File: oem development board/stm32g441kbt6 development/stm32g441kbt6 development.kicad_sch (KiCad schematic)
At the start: 22 parts, among them J1 CONN_pcie_x1, J2 Programming_Pin_Header, SW1 INTERRUPT TEST SWITCH, U1 STM32G441KBT6, U2 MCP2561-E_SN, U3 SPX3819M5-L-3-3_TR, Y1 X_Crystal_16MHz_18pF

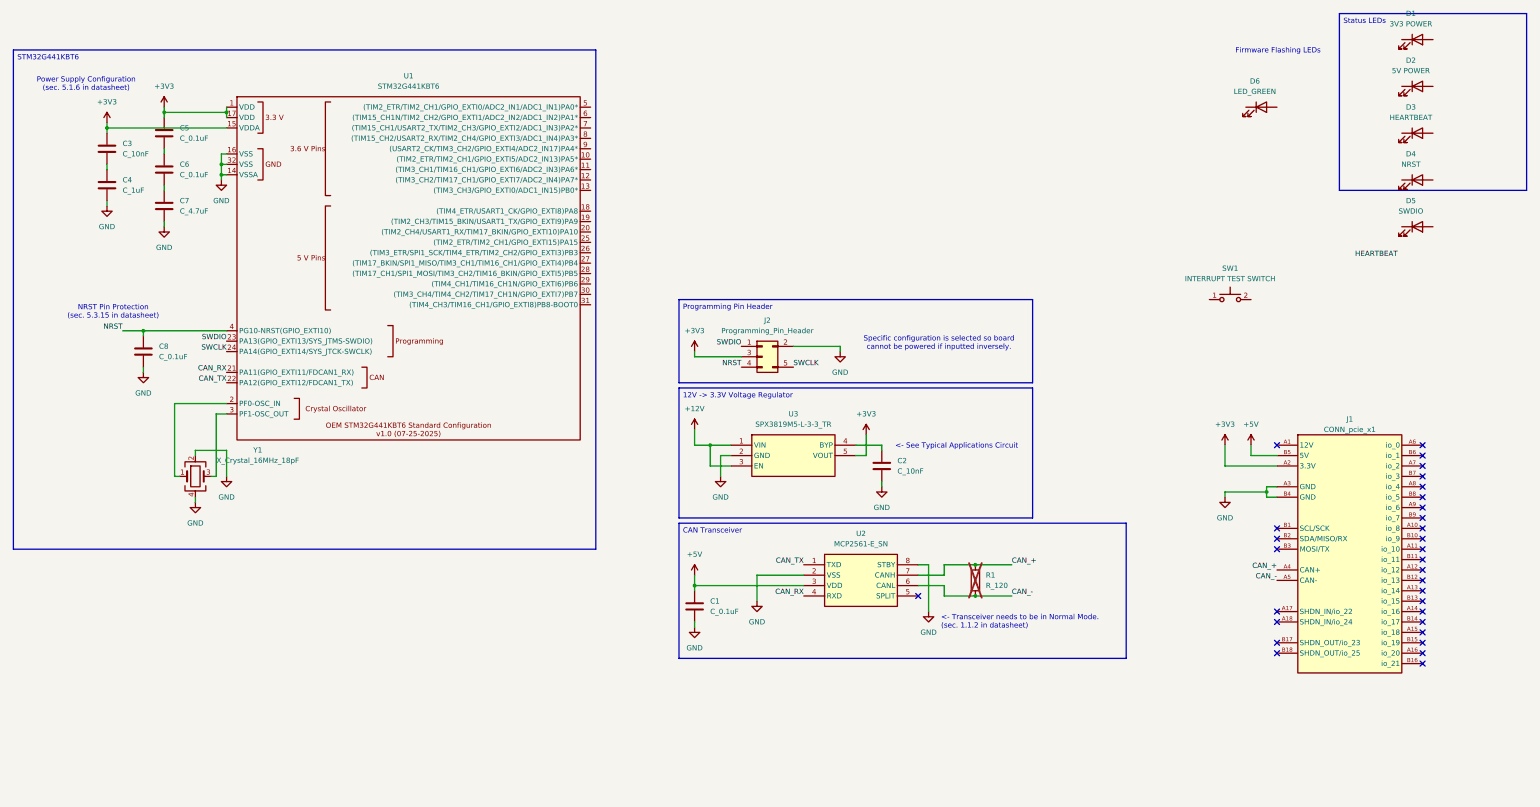
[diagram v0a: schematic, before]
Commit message: Added Debug LEDs, Some Test Points, Minor changes to STM32G441KBT6 symbol
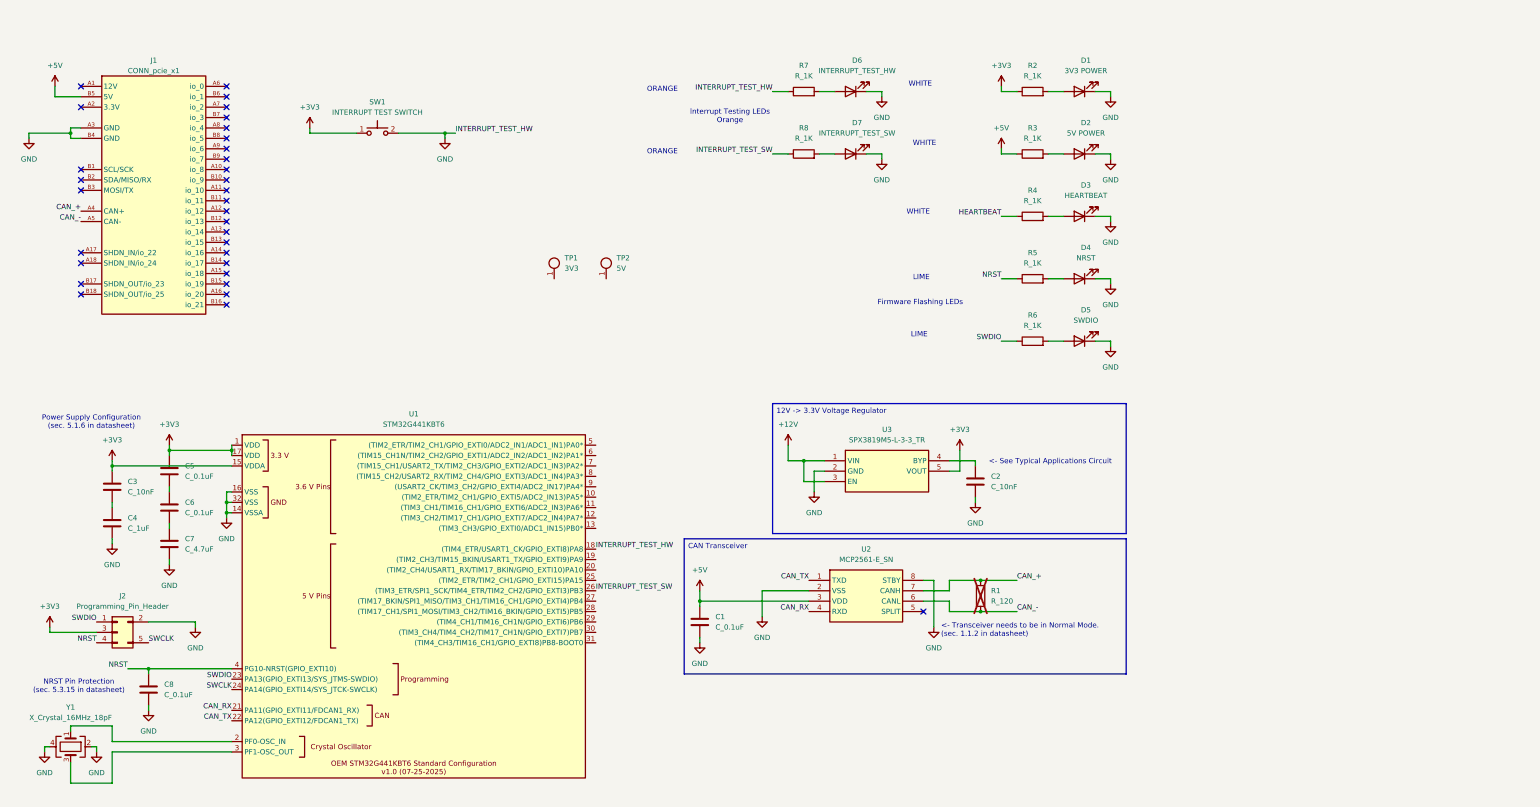
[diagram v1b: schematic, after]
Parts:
- removed D6: LED_GREEN, OEM:CHIPLED_0805, symbol OEM:LED_GREEN
- added D6: INTERRUPT_TEST_HW, OEM:CHIPLED_0805, symbol OEM:LED_AMBER
- added D7: INTERRUPT_TEST_SW, OEM:CHIPLED_0805, symbol OEM:LED_AMBER
- added R2, R3, R4, R5, R6, R7, R8: R_1K, OEM:R_0603, symbol OEM:R_1K
- added TP1: 3V3, OEM:Test_Point_SMD, symbol OEM:TP_SMD
- added TP2: 5V, OEM:Test_Point_SMD, symbol OEM:TP_SMD
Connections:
- net +3V3: now also SW1.1, R2.1; no longer J1.A2 (3.3V)
- net +5V: now also R3.1
- net GND: now also D1.1 (K), D2.1 (K), D3.1 (K), D4.1 (K), D5.1 (K), SW1.2, U1.18 ((TIM4_ETR/USART1_CK/GPIO_EXTI8)PA8), D6.1 (K), D7.1 (K), R7.1
- net HEARTBEAT: now also R4.1
- net NRST: now also R5.1
- net SWDIO: now also R6.1
- net at D2.2 (A): now also R3.2
- net at D3.2 (A): now also R4.2
- net at D4.2 (A): now also R5.2
- net at D1.2 (A): now also R2.2
- net INTERRUPT_TEST_SW: now reaches U1.26 ((TIM3_ETR/SPI1_SCK/TIM4_ETR/TIM2_CH2/GPIO_EXTI3)PB3)
- net INTERRUPT_TEST_SW: now also R8.1
- net at D5.2 (A): now also R6.2
- new net: D6.2 (A), R7.2
- new net: D7.2 (A), R8.2
- no-connect marks 31 -> 32
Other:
- note added: "Interrupt Testing LEDs Orange"
- note added: "LIME"
- note added: "ORANGE"
- note added: "WHITE"
- note removed: "Specific configuration is selected so board cannot be powered if inputted inversely."
- moved on the sheet: C1, C2, C3, C4, C5, C6, C7, C8, D1, D2, D3, D4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

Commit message: Condensed Symbol Design; Slight changes to development board
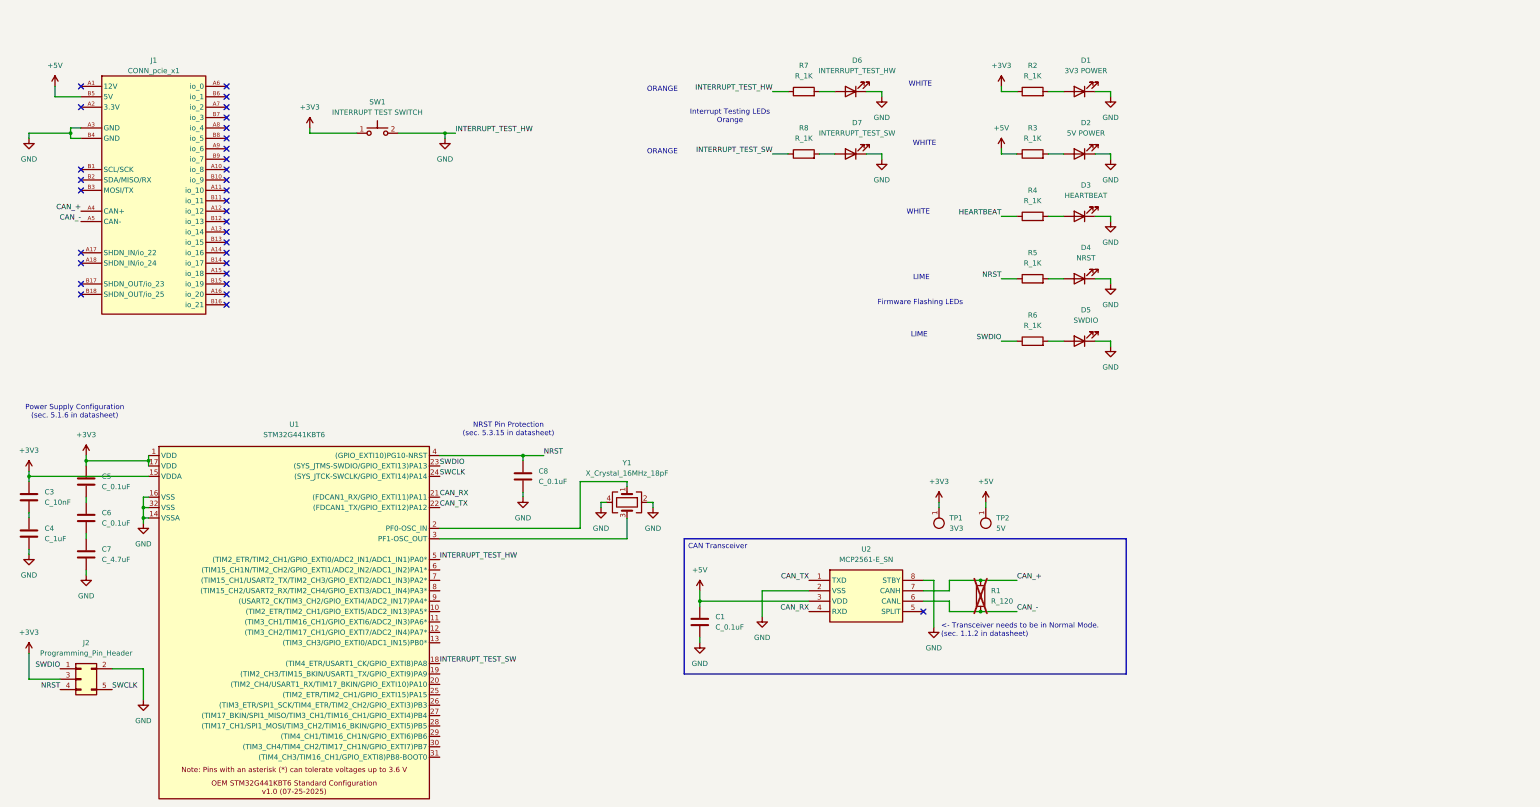
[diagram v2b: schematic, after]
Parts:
- removed C2: C_10nF, OEM:C_0603, symbol OEM:C_10nF
- removed U3: SPX3819M5-L-3-3_TR, stm32g441kbt6:SOIC127P600X175-8N, symbol stm32g441kb:SPX3819M5-L-3-3_TR
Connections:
- net +3V3: now also TP1.1
- net +5V: now also TP2.1
- net GND: now also U1.5 ((TIM2_ETR/TIM2_CH1/GPIO_EXTI0/ADC2_IN1/ADC1_IN1)PA0*); no longer U1.18 ((TIM4_ETR/USART1_CK/GPIO_EXTI8)PA8)
- net INTERRUPT_TEST_SW: now also U1.18 ((TIM4_ETR/USART1_CK/GPIO_EXTI8)PA8); no longer U1.26 ((TIM3_ETR/SPI1_SCK/TIM4_ETR/TIM2_CH2/GPIO_EXTI3)PB3)
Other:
- note removed: "<- See Typical Applications Circuit"
- moved on the sheet: C3, C4, C5, C6, C7, C8, J2, TP1, TP2, Y1

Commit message: Added footprints for new voltage regulator components, added test points and other things
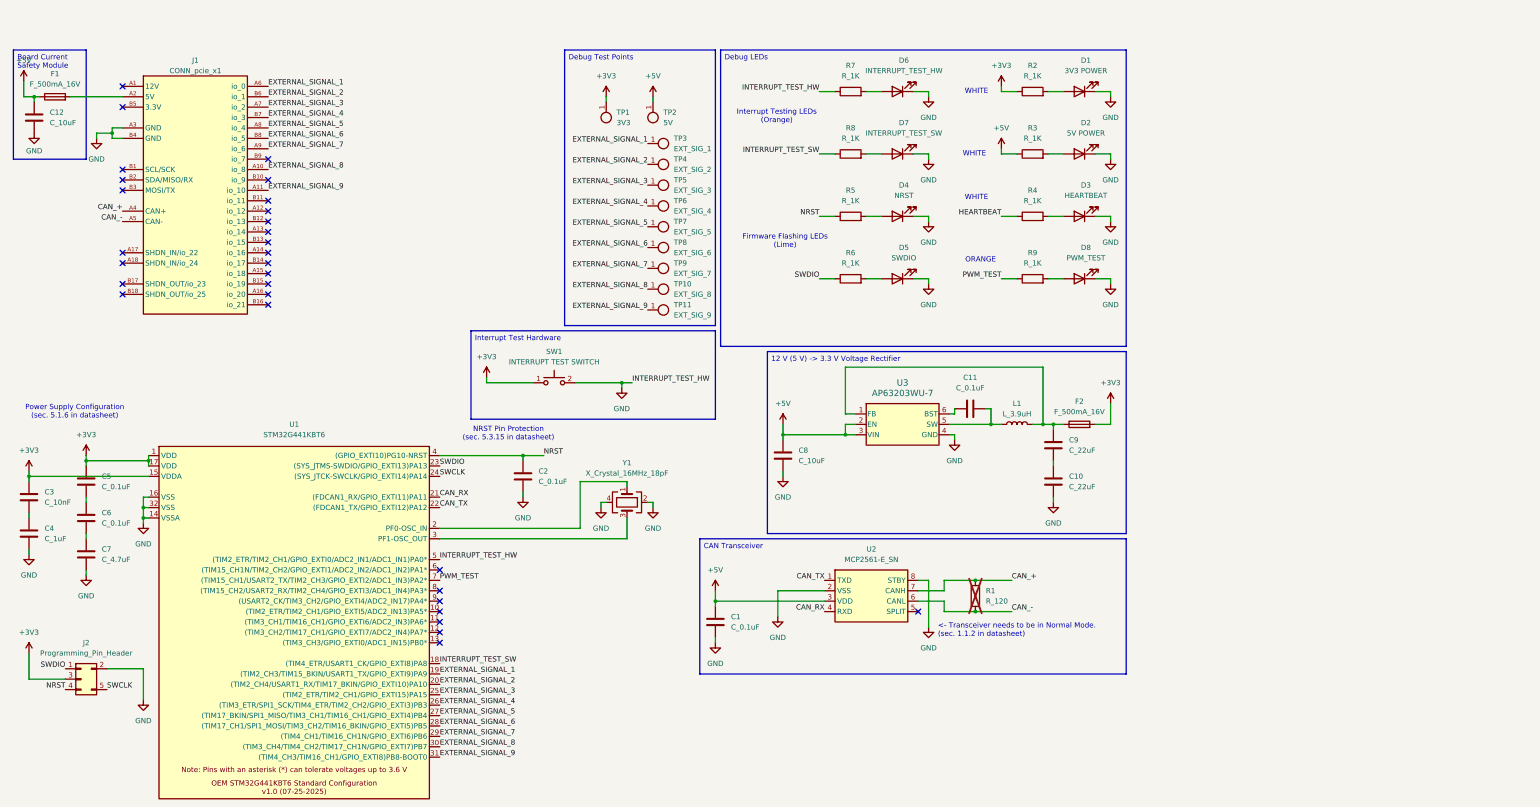
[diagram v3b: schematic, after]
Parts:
- added C10, C9: C_22uF, Capacitor_SMD:C_1206_3216Metric, symbol OEM:C_22uF
- added C11: C_0.1uF, OEM:C_0603, symbol OEM:C_0.1uF
- added C12, C8: C_10uF, OEM:C_0603, symbol OEM:C_10uF
- added D8: PWM_TEST, OEM:CHIPLED_0805, symbol OEM:LED_AMBER
- added F1, F2: F_500mA_16V, OEM:Fuse_1210, symbol OEM:F_500mA_16V
- added L1: L_3.9uH, stm32g441kbt6:IND_BOURNS_SRR5018, symbol stm32g441kb:L_3.9uH
- added R9: R_1K, OEM:R_0603, symbol OEM:R_1K
- added TP10: EXT_SIG_8, OEM:Test_Point_SMD, symbol OEM:TP_SMD
- added TP11: EXT_SIG_9, OEM:Test_Point_SMD, symbol OEM:TP_SMD
- added TP3: EXT_SIG_1, OEM:Test_Point_SMD, symbol OEM:TP_SMD
- added TP4: EXT_SIG_2, OEM:Test_Point_SMD, symbol OEM:TP_SMD
- added TP5: EXT_SIG_3, OEM:Test_Point_SMD, symbol OEM:TP_SMD
- added TP6: EXT_SIG_4, OEM:Test_Point_SMD, symbol OEM:TP_SMD
- added TP7: EXT_SIG_5, OEM:Test_Point_SMD, symbol OEM:TP_SMD
- added TP8: EXT_SIG_6, OEM:Test_Point_SMD, symbol OEM:TP_SMD
- added TP9: EXT_SIG_7, OEM:Test_Point_SMD, symbol OEM:TP_SMD
- added U3: AP63203WU-7, stm32g441kbt6:AP63203WU-7_DIO, symbol stm32g441kb:AP63203WU-7
- J1: footprint OEM:te_pcie_x1_connector -> OEM:pcie_x1
- renumbered C8 to C2
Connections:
- net +3V3: now also F2.2
- net +5V: now also C12.1, C8.1, F1.1, U3.2 (EN), U3.3 (VIN); no longer J1.B5 (5V)
- net GND: now also C10.2, C12.2, C8.2, D8.1 (K), U3.4 (GND)
- net EXTERNAL_SIGNAL_1: now reaches U1.19 ((TIM2_CH3/TIM15_BKIN/USART1_TX/GPIO_EXTI9)PA9)
- net EXTERNAL_SIGNAL_1: now also J1.A6 (io_0), TP3.1
- net EXTERNAL_SIGNAL_2: now reaches U1.20 ((TIM2_CH4/USART1_RX/TIM17_BKIN/GPIO_EXTI10)PA10)
- net EXTERNAL_SIGNAL_2: now also J1.B6 (io_1), TP4.1
- net EXTERNAL_SIGNAL_3: now reaches U1.25 ((TIM2_ETR/TIM2_CH1/GPIO_EXTI15)PA15)
- net EXTERNAL_SIGNAL_3: now also J1.A7 (io_2), TP5.1
- net EXTERNAL_SIGNAL_4: now reaches U1.26 ((TIM3_ETR/SPI1_SCK/TIM4_ETR/TIM2_CH2/GPIO_EXTI3)PB3)
- net EXTERNAL_SIGNAL_4: now also J1.B7 (io_3), TP6.1
- net EXTERNAL_SIGNAL_5: now reaches U1.27 ((TIM17_BKIN/SPI1_MISO/TIM3_CH1/TIM16_CH1/GPIO_EXTI4)PB4)
- net EXTERNAL_SIGNAL_5: now also J1.A8 (io_4), TP7.1
- net EXTERNAL_SIGNAL_6: now reaches U1.28 ((TIM17_CH1/SPI1_MOSI/TIM3_CH2/TIM16_BKIN/GPIO_EXTI5)PB5)
- net EXTERNAL_SIGNAL_6: now also J1.B8 (io_5), TP8.1
- net EXTERNAL_SIGNAL_7: now reaches U1.29 ((TIM4_CH1/TIM16_CH1N/GPIO_EXTI6)PB6)
- net EXTERNAL_SIGNAL_7: now also J1.A9 (io_6), TP9.1
- net EXTERNAL_SIGNAL_8: now reaches U1.30 ((TIM3_CH4/TIM4_CH2/TIM17_CH1N/GPIO_EXTI7)PB7)
- net EXTERNAL_SIGNAL_8: now also J1.A10 (io_8), TP10.1
- net EXTERNAL_SIGNAL_9: now reaches U1.31 ((TIM4_CH3/TIM16_CH1/GPIO_EXTI8)PB8-BOOT0)
- net EXTERNAL_SIGNAL_9: now also J1.A11 (io_10), TP11.1
- net PWM_TEST: now reaches U1.7 ((TIM15_CH1/USART2_TX/TIM2_CH3/GPIO_EXTI2/ADC1_IN3)PA2*)
- net PWM_TEST: now also R9.1
- net at J1.A2 (5V): now also F1.2
- new net: C9.1, F2.1, L1.2, U3.1 (FB)
- new net: C10.1, C9.2
- new net: D8.2 (A), R9.2
- new net: C11.2, L1.1, U3.5 (SW)
- new net: C11.1, U3.6 (BST)
- no-connect marks 32 -> 30
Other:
- note added: "Firmware Flashing LEDs (Lime)"
- note added: "Interrupt Testing LEDs (Orange)"
- note removed: "Firmware Flashing LEDs"
- note removed: "Interrupt Testing LEDs Orange"
- note removed: "LIME"
- moved on the sheet: C1, D4, D5, D6, D7, R1, R5, R6, R7, R8, SW1, TP1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

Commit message: Added 3D Models, Started PCB Design, Minor Fixes to Schematics
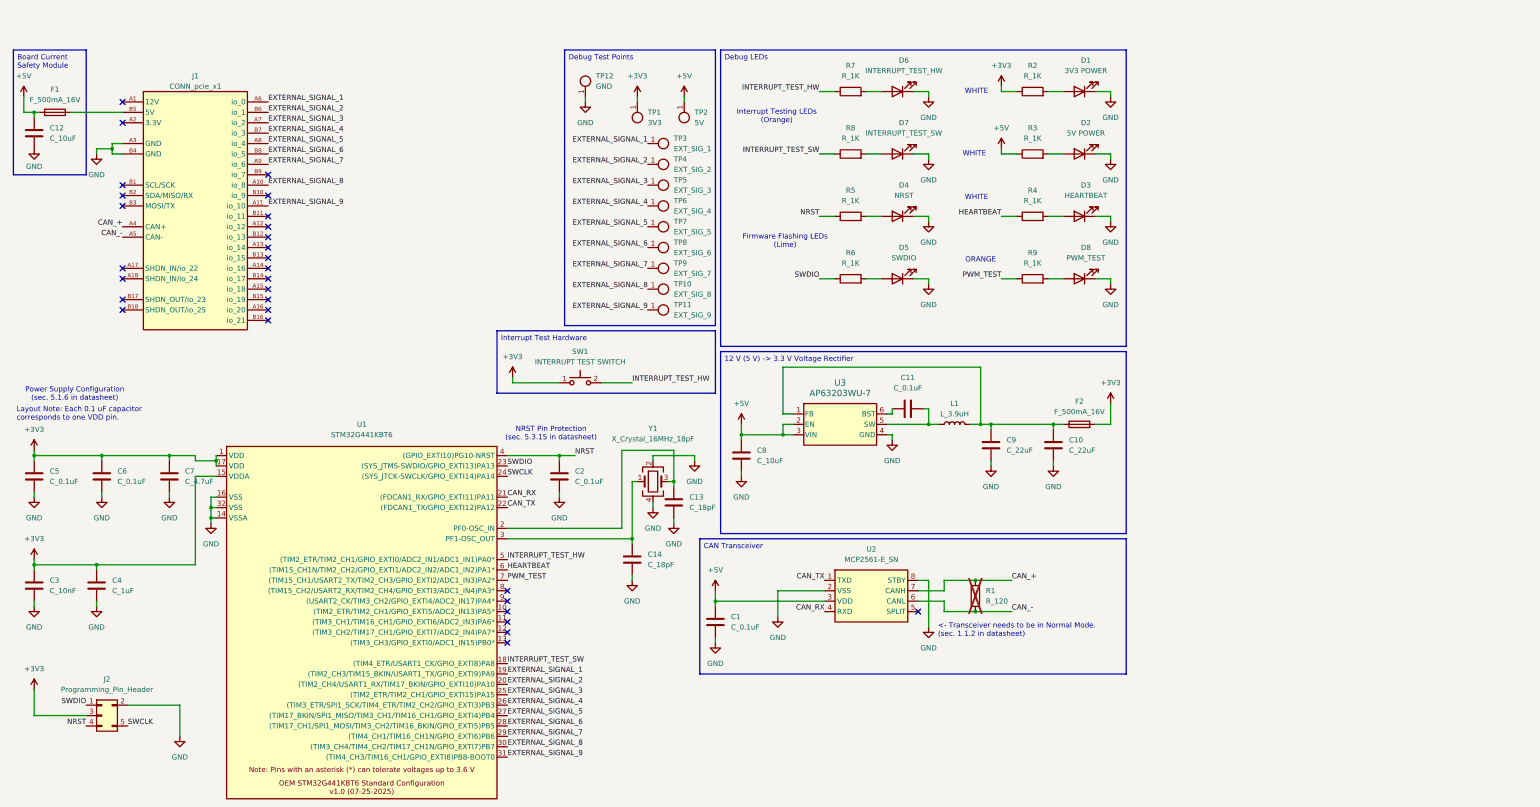
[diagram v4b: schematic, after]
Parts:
- added C13, C14: C_18pF, Capacitor_SMD:C_0805_2012Metric, symbol OEM:C_18pF
- added TP12: GND, OEM:Test_Point_SMD, symbol OEM:TP_SMD
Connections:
- net +3V3: now also C4.1, C6.1, C7.1
- net GND: now also C3.2, C5.2, C6.2, C9.2, C13.2, C14.2, TP12.1; no longer R7.1, SW1.2, U1.5 ((TIM2_ETR/TIM2_CH1/GPIO_EXTI0/ADC2_IN1/ADC1_IN1)PA0*)
- net HEARTBEAT: now also U1.6 ((TIM15_CH1N/TIM2_CH2/GPIO_EXTI1/ADC2_IN2/ADC1_IN2)PA1*)
- net at F1.2: now also J1.B5 (5V); no longer J1.A2 (5V)
- net at U1.2 (PF0-OSC_IN): now also Y1.3, C13.1; no longer Y1.1
- net at U1.3 (PF1-OSC_OUT): now also Y1.1, C14.1; no longer Y1.3
- net at C9.1, F2.1, L1.2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: now also C10.1
- new net INTERRUPT_TEST_HW: R7.1, SW1.2, U1.5 ((TIM2_ETR/TIM2_CH1/GPIO_EXTI0/ADC2_IN1/ADC1_IN1)PA0*)
- no-connect marks 30 -> 29
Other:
- note added: "Layout Note: Each 0.1 uF capacitor corresponds to one VDD pin."
- moved on the sheet: C10, C11, C12, C2, C3, C4, C5, C6, C7, C8, C9, F1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
